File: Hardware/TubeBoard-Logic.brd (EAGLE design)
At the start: 71.1 x 76.2 mm, 35 parts, among them IC1 74HC373DW, IC2 74HC373DW, IC3 74HC85D, IC4 74HC04D, IC5 74HC08D, T1 MPSA42, T2 MPSA42

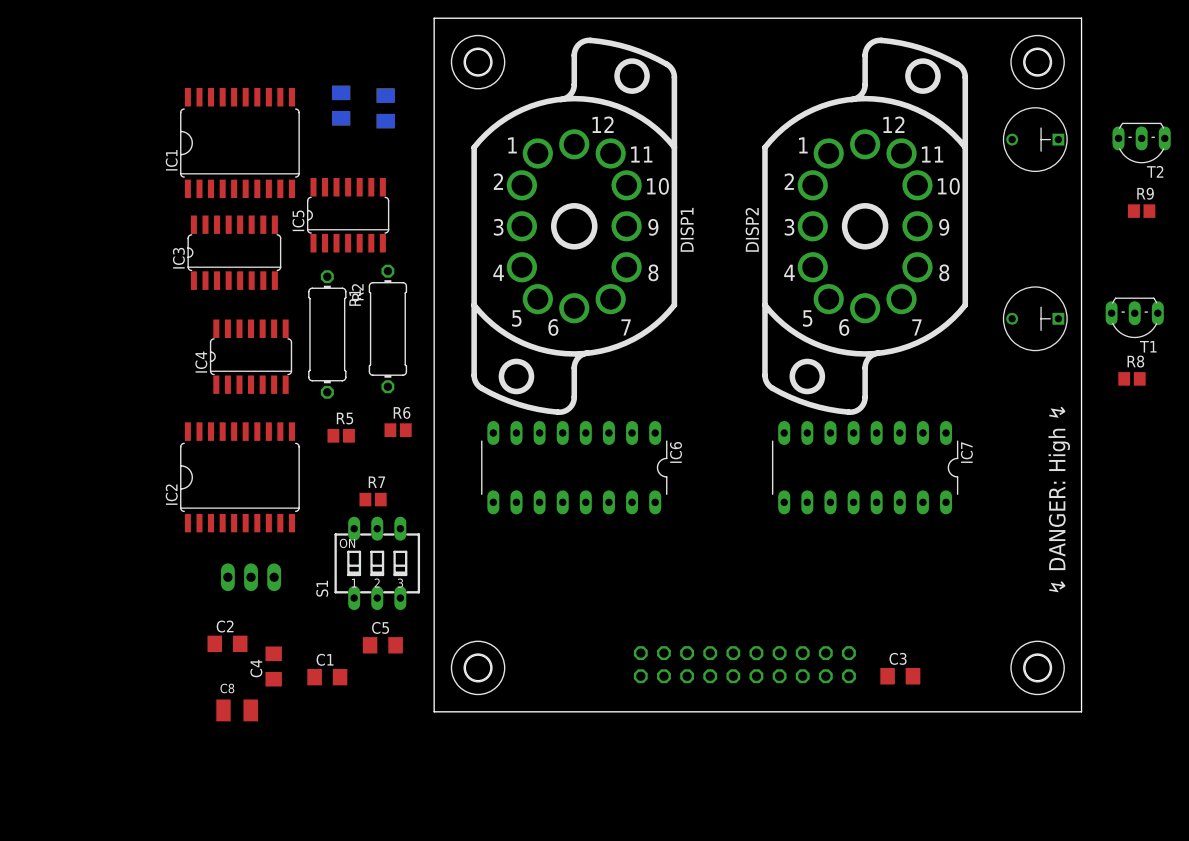
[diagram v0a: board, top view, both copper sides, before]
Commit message: separated tubes and logic on two separate boards
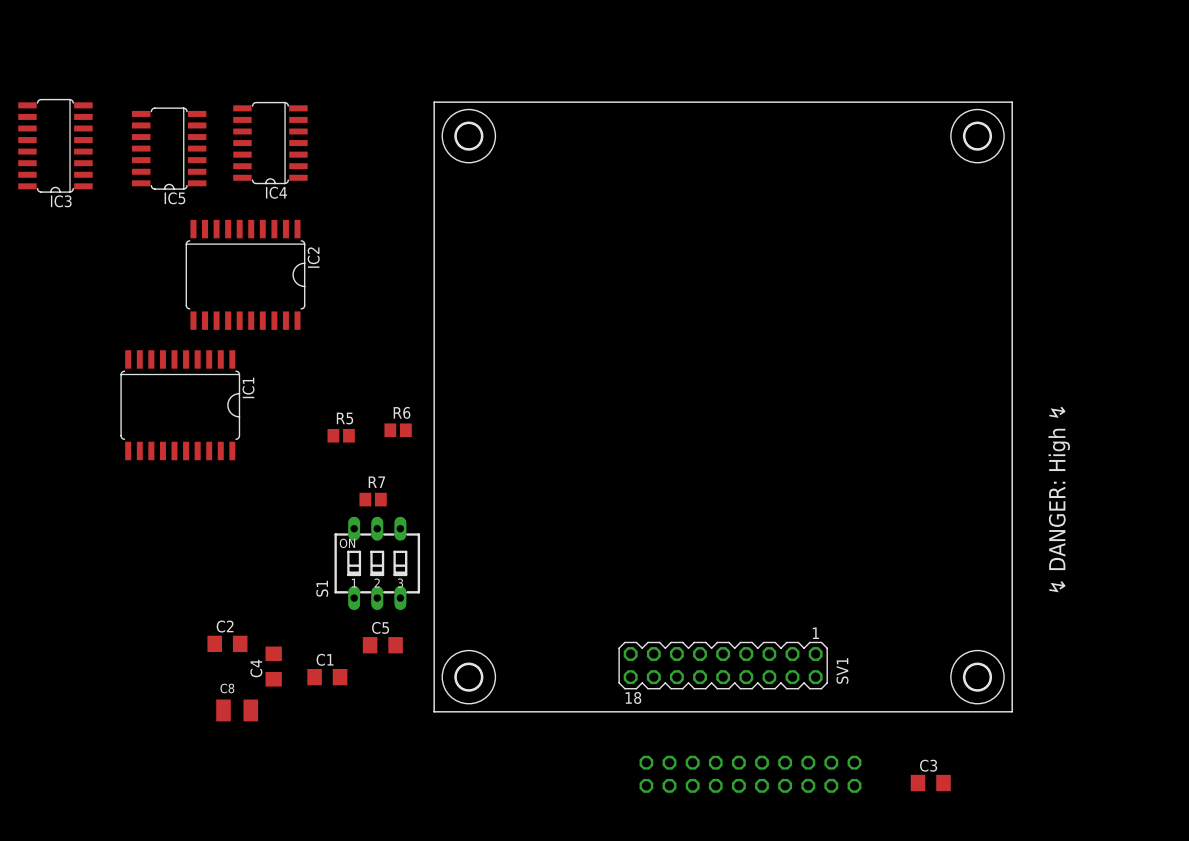
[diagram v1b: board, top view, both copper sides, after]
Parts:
- removed DISP1, DISP2: DISP_IN12A, dp_devices:DISP_IN-12_SOCKET
- removed IC6, IC7: (no value), Parts:DIL16
- removed R1, R2: 15k, rcl:0411/12
- removed R3, R4: 174k, rcl:M1206
- removed R8, R9: 10k, rcl:R2012
- removed T1, T2: MPSA42, transistor:TO92-EBC
- removed U$1, U$2: INS-1, Parts:INS-1
- SV1: device con-lstb:MA03-1 -> con-lstb:MA09-2
- moved SV1 52.8 mm to (31.8, 5.08), flipped to the top, turned to 180 degrees
- moved IC1 29.5 mm to (-27.9, 33.7), turned to 180 degrees
- moved IC4 23.6 mm to (-18.0, 62.5), turned to 90 degrees
- moved IC3 22.9 mm to (-41.6, 62.2), turned to 90 degrees
- moved IC2 22.3 mm to (-20.7, 48.0), turned to 180 degrees
- moved IC5 21.0 mm to (-29.1, 61.9), turned to 90 degrees
- moved C3 12.2 mm to (54.6, -7.82)
- moved SV2 12.1 mm to (34.7, -6.86)
- moved H4 10.5 mm to (59.7, 63.2)
- moved H3 8.19 mm to (3.81, 63.2)
- moved H2 6.68 mm to (59.7, 3.81)
- moved H1 1.44 mm to (3.81, 3.81)
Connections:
- removed net 1_K0: DISP1.2, IC6.16
- removed net 1_K1: DISP1.11, IC6.15
- removed net 1_K2: DISP1.10, IC6.8
- removed net 1_K3: DISP1.9, IC6.9
- removed net 1_K4: DISP1.8, IC6.13
- removed net 1_K5: DISP1.7, IC6.14
- removed net 1_K6: DISP1.6, IC6.11
- removed net 1_K7: DISP1.5, IC6.10
- removed net 1_K8: DISP1.4, IC6.1
- removed net 1_K9: DISP1.3, IC6.2
- removed net 2_K0: DISP2.2, IC7.16
- removed net 2_K1: DISP2.11, IC7.15
- removed net 2_K2: DISP2.10, IC7.8
- removed net 2_K3: DISP2.9, IC7.9
- removed net 2_K4: DISP2.8, IC7.13
- removed net 2_K5: DISP2.7, IC7.14
- removed net 2_K6: DISP2.6, IC7.11
- removed net 2_K7: DISP2.5, IC7.10
- removed net 2_K8: DISP2.4, IC7.1
- removed net 2_K9: DISP2.3, IC7.2
- removed net HV_ANODE: R1.2, R2.2, R3.1, R4.1, SV1.2
- removed net K_COLON_B: T1.C, U$2.C
- removed net K_COLON_T: T2.C, U$1.C
- removed net N$1: DISP1.1, R1.1
- removed net N$2: DISP2.1, R2.1
- removed net N$3: R3.2, U$1.A
- removed net N$4: R4.2, U$2.A
- removed net N$5: R8.2, T1.B
- removed net N$6: R9.2, T2.B
- net +5V: now also SV1.17, SV1.18; no longer IC6.5, IC7.5
- net COLON_B: now also SV1.8; no longer R8.1
- net COLON_T: now also SV1.6; no longer R9.1
- net DRIVE_HI: now also SV1.3
- net DRIVE_LO: now also SV1.7
- net DRIVE_MED: now also SV1.5
- net GND: now also SV1.2, SV1.4; no longer IC6.12, IC7.12, SV1.3, T1.E, T2.E
- net LDIGIT0: now also SV1.16; no longer IC6.3
- net LDIGIT1: now also SV1.14; no longer IC6.6
- net LDIGIT2: now also SV1.12; no longer IC6.7
- net LDIGIT3: now also SV1.10; no longer IC6.4
- net RDIGIT0: now also SV1.15; no longer IC7.3
- net RDIGIT1: now also SV1.13; no longer IC7.6
- net RDIGIT2: now also SV1.11; no longer IC7.7
- net RDIGIT3: now also SV1.9; no longer IC7.4
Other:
- board size 71.1 x 76.2 mm -> 63.5 x 67 mm

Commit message: routed tube logic board
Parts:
- added SV3: (no value), con-lstb:MA10-2
- added WEED1: WEED, Parts:DOINK
- moved IC3 94.5 mm to (52.4, 52.8), flipped to the bottom, turned to 270 degrees
- moved C8 71.0 mm to (15.3, 60.8), turned to 180 degrees
- moved SV2 69.4 mm to (31.8, 62.5)
- moved C3 69.0 mm to (49.5, 61.0), flipped to the bottom, turned to 90 degrees
- moved IC5 66.7 mm to (34.9, 43.2), turned to 0 degrees
- moved IC2 65.6 mm to (38.7, 20.3), turned to 90 degrees
- moved S1 64.1 mm to (53.1, 40.5), flipped to the bottom, turned to 270 degrees
- moved C4 61.2 mm to (28.6, 45.1), turned to 270 degrees
- moved IC4 60.0 mm to (34.9, 34.3), turned to 180 degrees
- moved R5 55.8 mm to (45.1, 37.9), flipped to the bottom
- moved R7 55.4 mm to (45.1, 43.0), flipped to the bottom
- moved IC1 54.3 mm to (24.8, 20.3), turned to 90 degrees
- moved C5 54.0 mm to (42.5, 31.8)
- moved R6 50.0 mm to (45.1, 40.5), flipped to the bottom
- moved C1 47.4 mm to (34.9, 12.1)
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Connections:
- net !NIXIE_CS: now also SV3.17
- net +5V: now also SV3.19
- net A0: now also SV3.3
- net A1: now also SV3.5
- net A2: now also SV3.7
- net A3: now also SV3.9
- net A4: now also SV3.11
- net D0: now also SV3.8
- net D1: now also SV3.6
- net D2: now also SV3.4
- net D3: now also SV3.10
- net D4: now also SV3.12
- net D5: now also SV3.14
- net D6: now also SV3.16
- net D7: now also SV3.18
- net GND: now also SV3.1, SV3.2, SV3.20
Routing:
- net +5V: track 0.00 -> 165.8 mm, vias 0 -> 5
- net D0: track 0.00 -> 80.1 mm, vias 0 -> 3
- net D1: track 0.00 -> 77.8 mm, vias 0 -> 3
- net D2: track 0.00 -> 73.6 mm, vias 0 -> 3
- net D7: track 0.00 -> 67.3 mm
- net D3: track 0.00 -> 65.6 mm
- net D4: track 0.00 -> 63.9 mm, vias 0 -> 3
- net D6: track 0.00 -> 63.2 mm, vias 0 -> 3
- net D5: track 0.00 -> 58.1 mm, vias 0 -> 2
- net LDIGIT3: track 0.00 -> 50.9 mm, vias 0 -> 1
- net A0: track 0.00 -> 41.0 mm, vias 0 -> 2
- net LDIGIT2: track 0.00 -> 40.5 mm, vias 0 -> 1
- net !NIXIE_CS: track 0.00 -> 37.4 mm, vias 0 -> 1
- net SELECT_EN: track 0.00 -> 35.6 mm, vias 0 -> 1
- net A4: track 0.00 -> 32.3 mm
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- added copper zone on layer 1, net GND
- added copper zone on layer 16, net GND
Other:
- board text added: "Address Selector"
- board text added: "IN-12 Driver Logic (c) 2019 Tristan Seifert"
- board text removed: "IN-12A Serial Driver (c) 2019 Tristan Seifert"

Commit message: added data bus resistors; better reset circuit
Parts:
- IC4: value 74HC04D -> 74HC08D
- IC5: value 74HC08D -> 74HC04D
- moved C1 51.0 mm to (49.5, 61.0), flipped to the bottom, turned to 90 degrees
- moved C3 51.0 mm to (34.9, 12.1), flipped to the top, turned to 0 degrees
- moved C2 33.3 mm to (28.6, 45.1), turned to 270 degrees
- moved C4 33.3 mm to (15.2, 14.6), turned to 180 degrees
- moved IC4 8.89 mm to (34.9, 43.2), turned to 0 degrees
- moved IC5 8.89 mm to (34.9, 34.3), turned to 180 degrees
- renumbered C8 to C6, R5 to R1, R6 to R2, R7 to R3
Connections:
- net !A0: now also IC4.5, IC5.4; no longer IC4.4, IC5.5
- net !NIXIE_CS: now also IC5.1; no longer IC4.1
- net A0: now also IC4.2, IC5.3; no longer IC4.3, IC5.2
- net BOARD_SELECT: now also IC4.1, IC4.4, IC4.8; no longer IC5.1, IC5.4, IC5.8
- net CONTROL_LATCH: now also IC4.3; no longer IC5.3
- net DIGIT_LATCH: now also IC4.6; no longer IC5.6
- net NIXIE_CS: now also IC4.9, IC5.2; no longer IC4.2, IC5.9
- net SELECT_EN: now also IC4.10; no longer IC5.10

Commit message: tied unused logic on tube board logic board to ground
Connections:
- net GND: now also IC4.12, IC4.13, IC5.11, IC5.13, IC5.5, IC5.9
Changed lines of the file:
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@@
 <via x="40.005" y="17.78" extent="1-16" drill="0.35"/>
 <via x="38.1" y="15.875" extent="1-16" drill="0.35"/>
+<contactref element="IC5" pad="5"/>
+<contactref element="IC5" pad="13"/>
+<contactref element="IC5" pad="9"/>
+<contactref element="IC5" pad="11"/>
+<contactref element="IC4" pad="12"/>
+<contactref element="IC4" pad="13"/>
 </signal>
 <signal name="COLON_T">

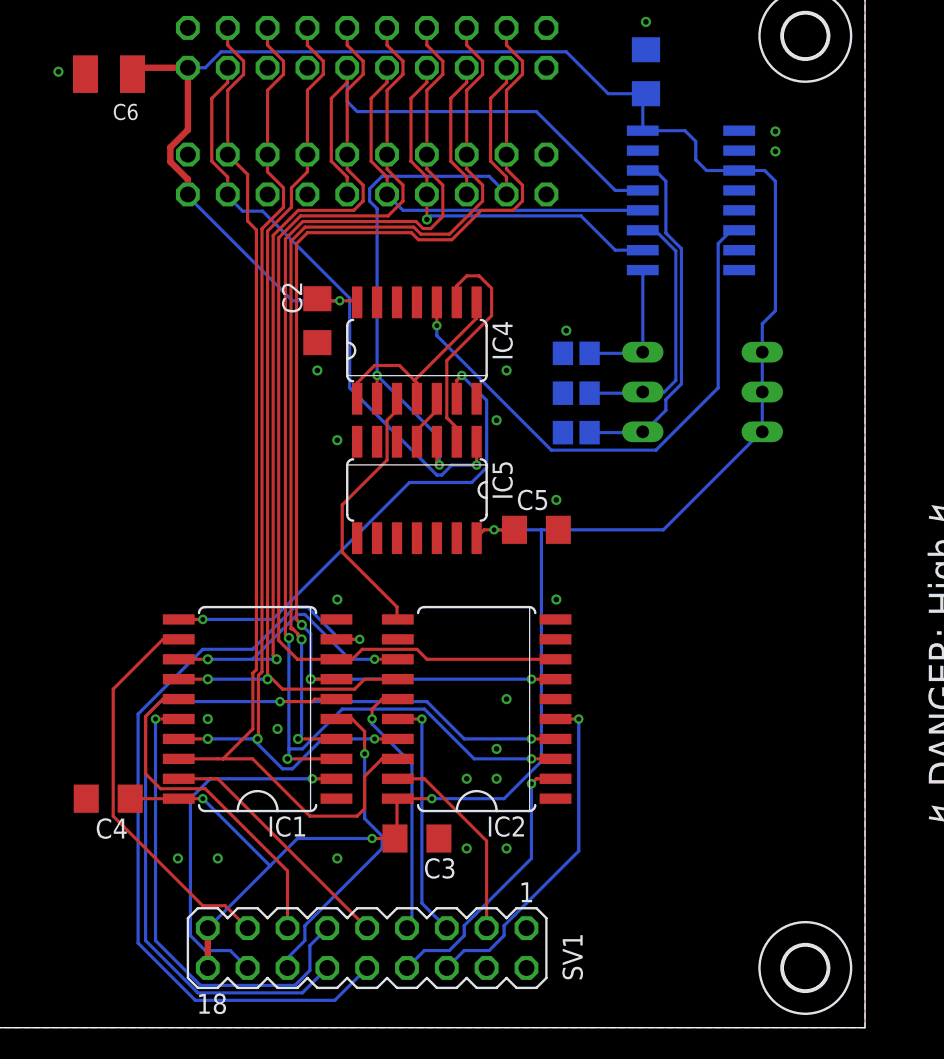
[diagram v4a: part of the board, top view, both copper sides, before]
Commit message: added ARM chip to driver boards to PWM tubes
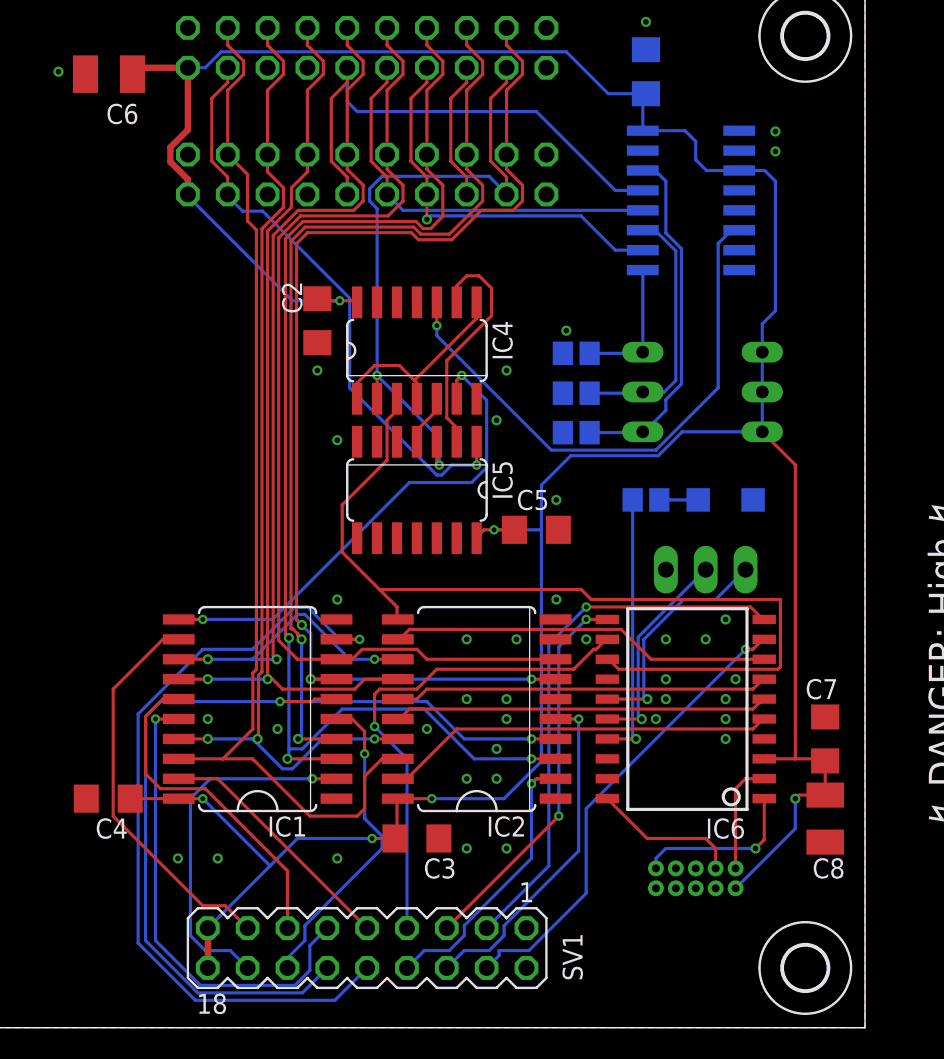
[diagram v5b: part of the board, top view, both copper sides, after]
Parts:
- added C7: 100nF, rcl:C1206
- added C8: 10µF, rcl:SMC_B
- added IC6: MKE04Z8, Parts:SOIC20S
- added J1: CORTEX_DEBUG_PTH, SparkFun-Connectors:2X5-PTH-1.27MM
- added LED1: (no value), led:CHIPLED_1206
- added R4: 3k, rcl:R2012
- added SV4: (no value), con-lstb:MA03-1
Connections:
- removed net DRIVE_HI: IC2.19, SV1.3
- removed net DRIVE_LO: IC2.15, SV1.7
- removed net DRIVE_MED: IC2.16, SV1.5
- new net !ARM_RESET: IC6.1, J1.10
- new net ARM_SWDCLK: IC6.20, J1.4
- new net ARM_SWDIO: IC6.2, J1.2
- new net DRIVE0: IC2.12, IC6.8
- new net DRIVE1: IC2.15, IC6.7
- new net DRIVE2: IC2.16, IC6.6
- new net DRIVE3: IC2.19, IC6.5
- new net N$9: LED1.A, R4.2
- new net PWM0: IC6.12, SV1.7
- new net PWM1: IC6.11, SV1.5
- new net PWM2: IC6.10, SV1.3
- new net PWM3: IC6.9, SV1.4
- new net STATUS0: IC6.17, R4.1
- new net UART_RX: IC6.16, SV4.2
- new net UART_TX: IC6.15, SV4.3
- net +5V: now also C7.1, C8.+, IC6.3, J1.1
- net CONTROL_LATCH: now also IC6.13
- net GND: now also C7.2, C8.-, IC6.4, J1.3, J1.5, J1.9, LED1.C, SV4.1; no longer SV1.4
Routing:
- net CONTROL_LATCH: track 17.0 -> 58.5 mm
- net +5V: track 165.8 -> 204.6 mm, vias 5 -> 6
- net PWM2: track 0.00 -> 34.8 mm, vias 0 -> 1
- net PWM0: track 0.00 -> 32.1 mm, vias 0 -> 1
- net PWM3: track 0.00 -> 29.7 mm, vias 0 -> 1
- net DRIVE3: track 0.00 -> 24.9 mm
- net PWM1: track 0.00 -> 24.7 mm, vias 0 -> 2
- net DRIVE0: track 0.00 -> 24.4 mm
- net DRIVE2: track 0.00 -> 23.9 mm
- net DRIVE1: track 0.00 -> 23.9 mm
- net STATUS0: track 0.00 -> 17.2 mm, vias 0 -> 1
- net DRIVE_LO: track 17.1 -> 0.00 mm, vias 1 -> 0
- net DRIVE_MED: track 15.5 -> 0.00 mm, vias 1 -> 0
- net UART_TX: track 0.00 -> 14.9 mm, vias 0 -> 1
- net UART_RX: track 0.00 -> 13.7 mm, vias 0 -> 1
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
